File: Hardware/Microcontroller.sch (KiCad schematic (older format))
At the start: 4 parts

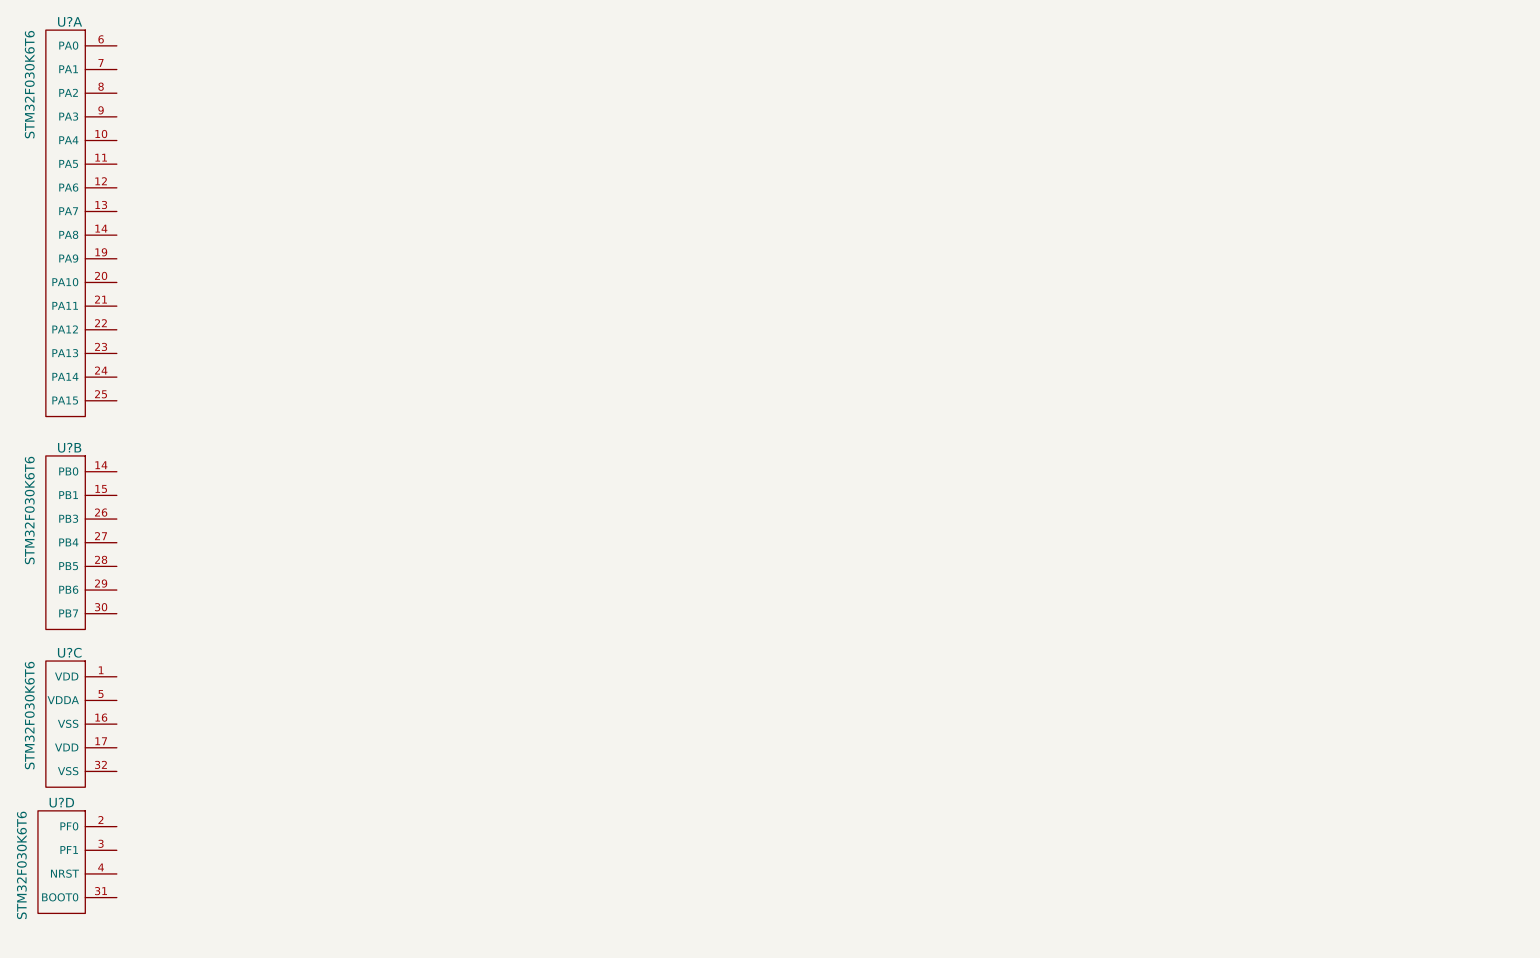
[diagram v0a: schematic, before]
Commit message: Added LDC to schematic
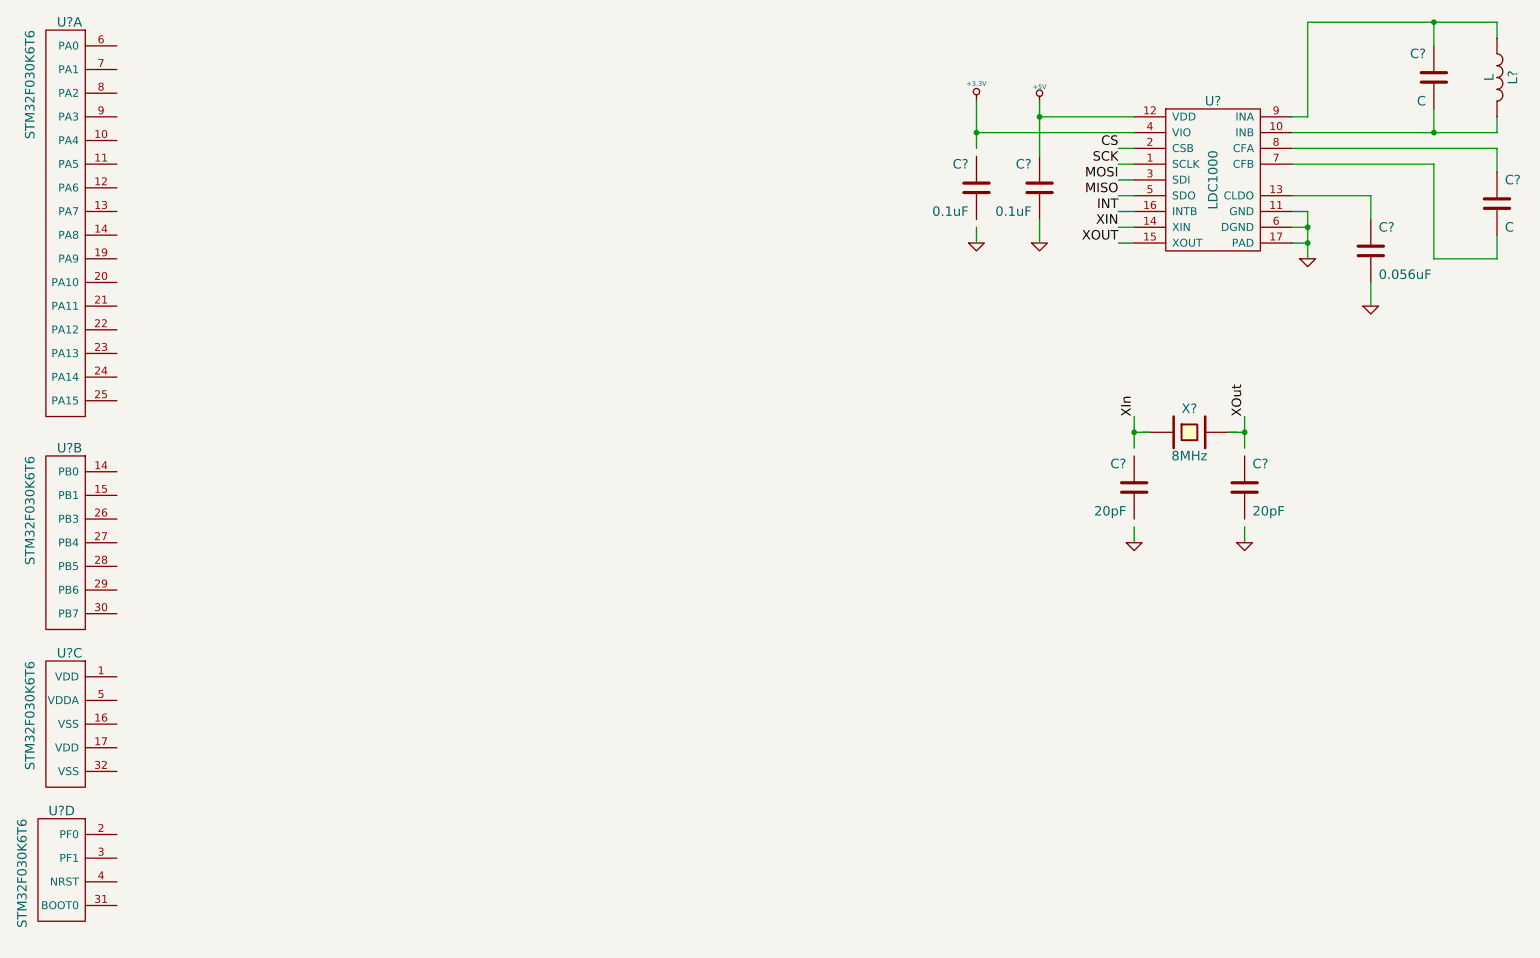
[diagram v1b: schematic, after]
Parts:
- added C? (x2): C, ~, symbol C
- added C?: 0.056uF, CAPC1608-N, symbol C
- added C? (x2): 0.1uF, CAPC1608-N, symbol C
- added C? (x2): 20pF, CAPC1608-N, symbol C
- added L?: L, ~, symbol L
- added U?: LDC1000, ~, symbol LDC1000
- added X?: 8MHz, ~, symbol CRYSTAL
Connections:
- net labels added: +3.3V, +5V, CS, GND, INT, MISO, MOSI, SCK, XIN, XIn, XOUT, XOut
- wire segments 0 -> 40
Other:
- moved on the sheet: U?D
